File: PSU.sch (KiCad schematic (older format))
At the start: 45 parts, among them J10 1053091202, Q5 BSS84PH6327XTSA2, Q6 IRF7416TRPBF, U13 AP62301WU-7, U14 AP62301WU-7, U15 AP62301WU-7, U16 LMV431IM5, U17 AP62301WU-7

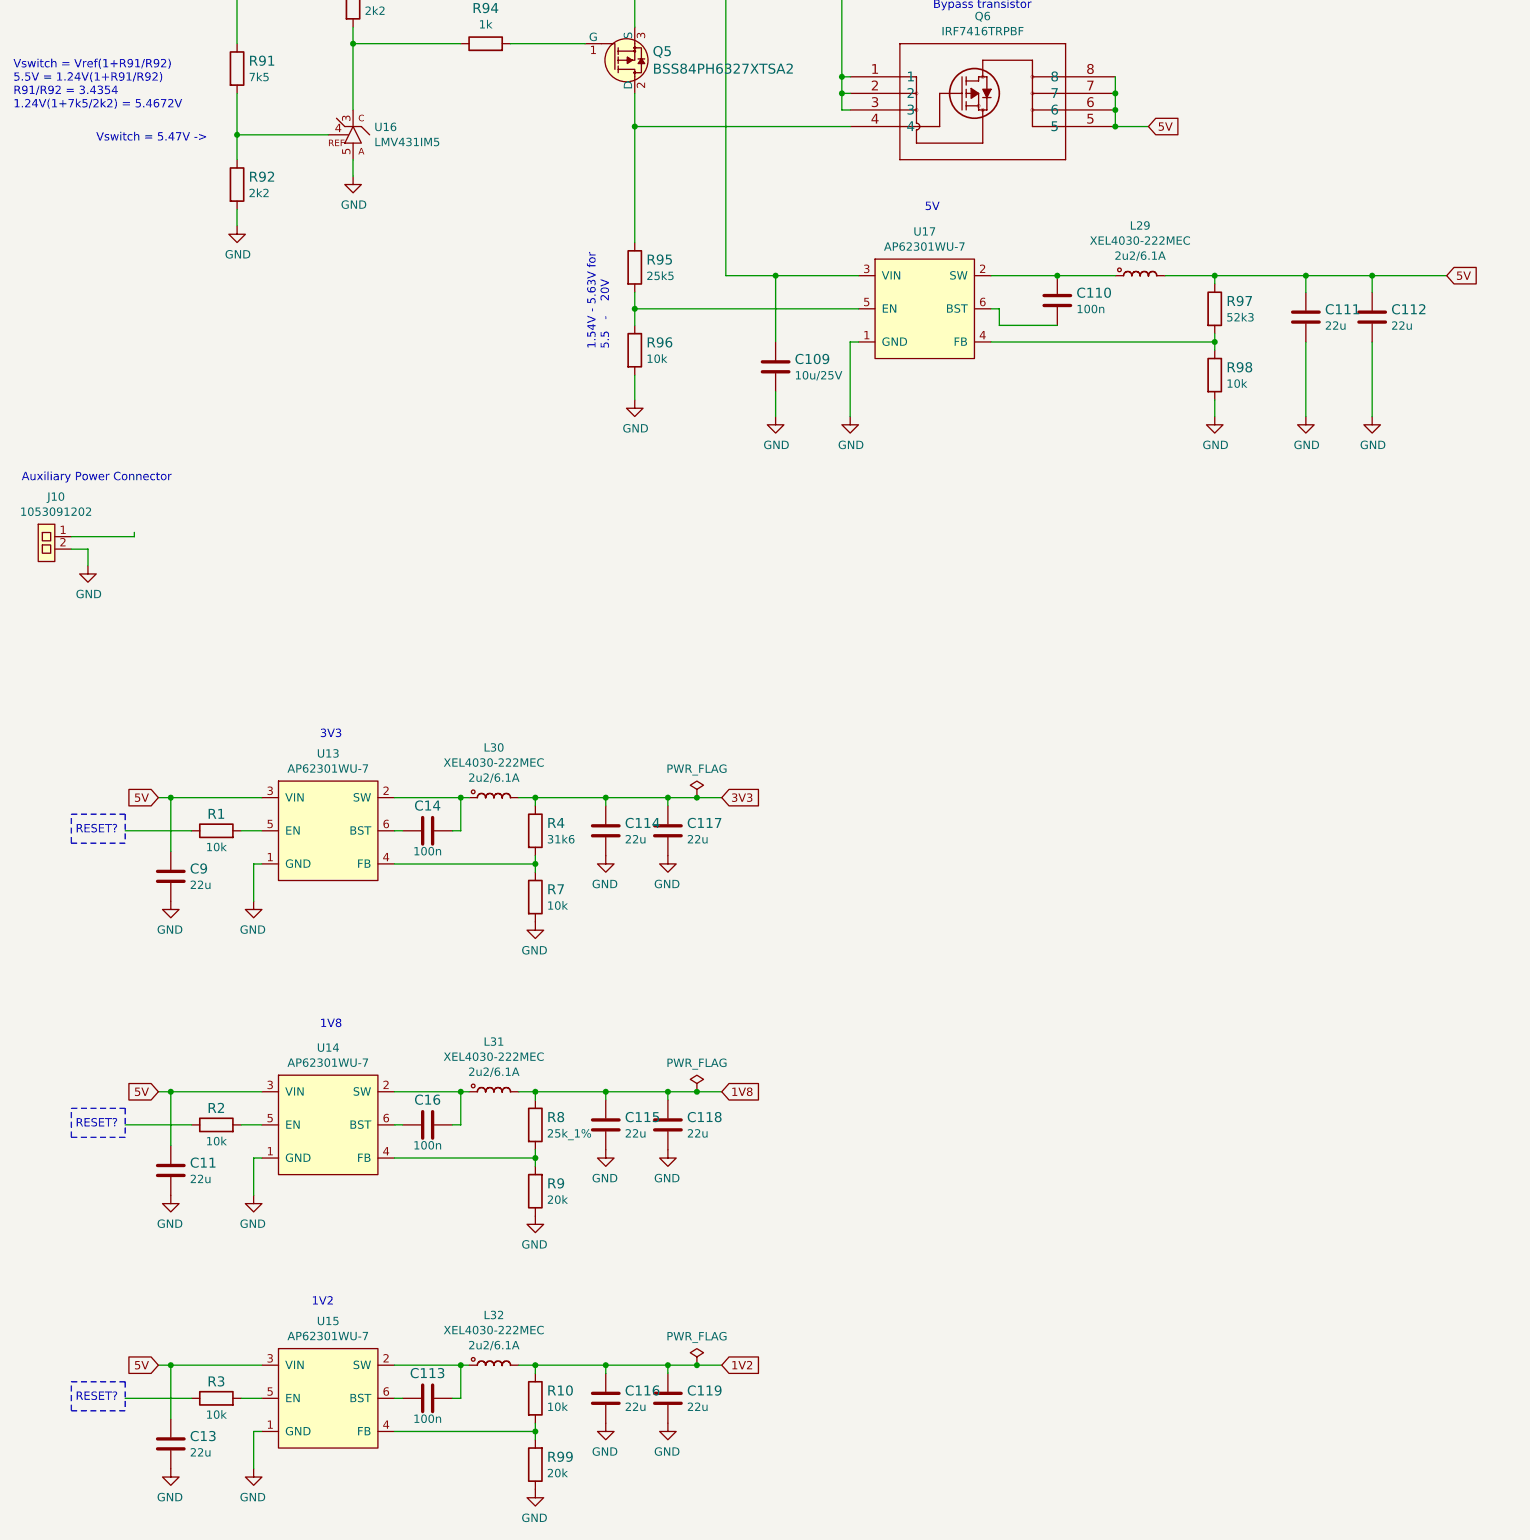
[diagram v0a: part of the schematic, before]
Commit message: Cleanup PoE.sch, change names of power lines
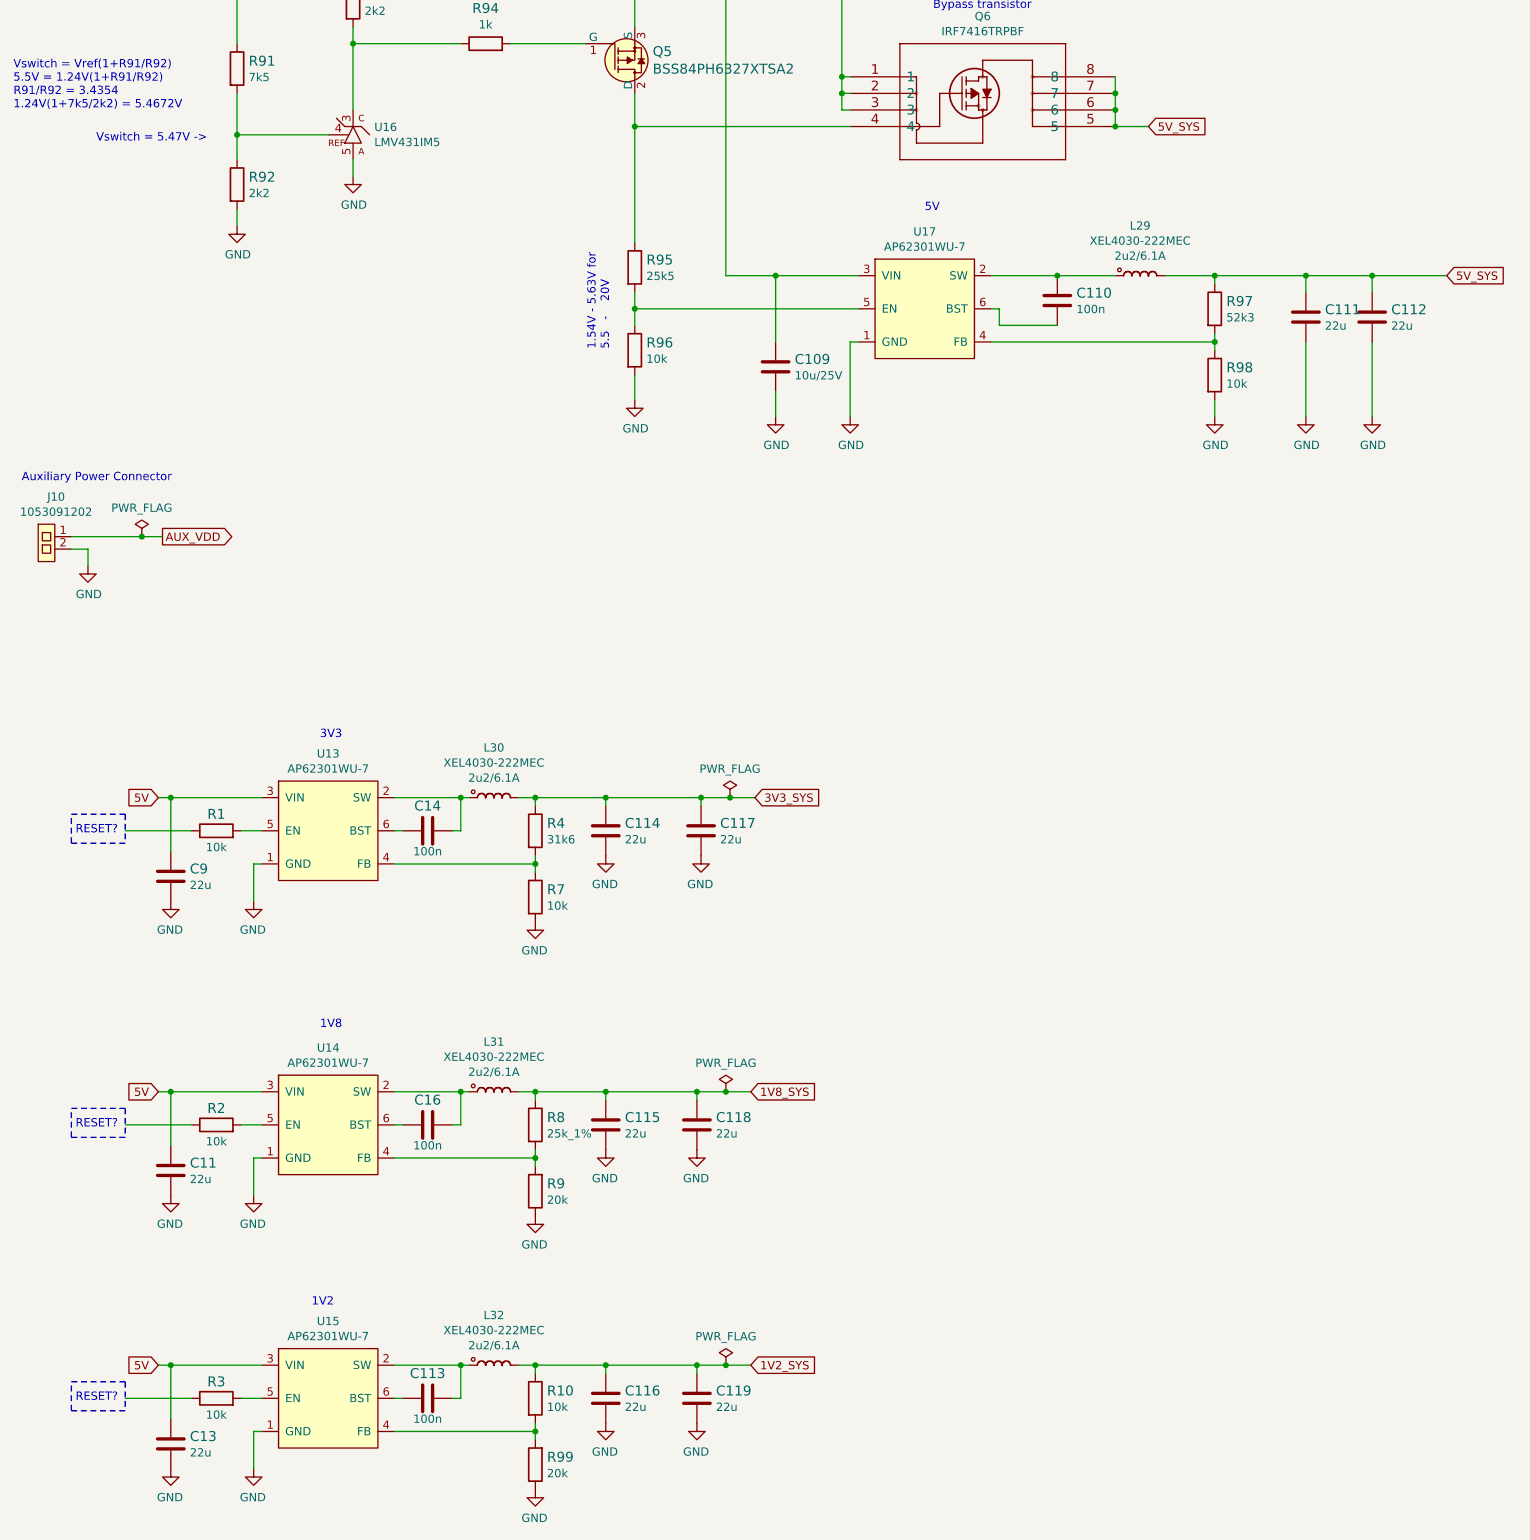
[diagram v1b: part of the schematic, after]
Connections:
- net labels added: 1V2_SYS, 1V8_SYS, 3V3_SYS, 5V_SYS, AUX_VDD
- net labels removed: 1V2, 1V8, 3V3
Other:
- moved on the sheet: C117, C118, C119
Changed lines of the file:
@@
 Auxiliary Power Connector
-Wire Wire Line
-	1580 4575 1580 4549
-Wire Wire Line
-	1200 4575 1580 4575
 Wire Wire Line
 	1300 4650 1200 4650
@@
 $EndComp
 Text GLabel 7700 2100 2    50   Input ~ 0
-5V
+5V_SYS
 $Comp
 L sa800u-baseboard-hw:C_100n_0402 C110
@@
 Connection ~ 9050 3000
 Text GLabel 9500 3000 2    50   Input ~ 0
-5V
+5V_SYS
 Wire Wire Line
 	7800 3000 8100 3000
@@
 	1    0    0    -1
 $EndComp
-Wire Wire Line
-	4425 9575 4800 9575
-Connection ~ 4800 9575
-Wire Wire Line
-	4800 9625 4800 9575
 $Comp
 L sa800u-baseboard-hw:GND #PWR0188
 U 1 1 61E1B2C0
-P 4800 9925
+P 4975 9925
 AR Path="/61B0DC30/61E1B2C0" Ref="#PWR0188"  Part="1"
 AR Path="/61DC2BE0/61E1B2C0" Ref="#PWR0176"  Part="1"
-F 0 "#PWR0188" H 4800 9675 50  0001 C CNN
-F 1 "GND" H 4805 9752 50  0000 C CNN
-F 2 "" H 4800 9925 50  0001 C CNN
-F 3 "" H 4800 9925 50  0001 C CNN
-	1    4800 9925
+F 0 "#PWR0188" H 4975 9675 50  0001 C CNN
+F 1 "GND" H 4980 9752 50  0000 C CNN
+F 2 "" H 4975 9925 50  0001 C CNN
+F 3 "" H 4975 9925 50  0001 C CNN
+	1    4975 9925
 	-1   0    0    -1
 $EndComp
@@
 L sa800u-baseboard-hw:C_22u_0603 C119
 U 1 1 61E1B2BF
-P 4800 9775
+P 4975 9775
 AR Path="/61B0DC30/61E1B2BF" Ref="C119"  Part="1"
 AR Path="/61DC2BE0/61E1B2BF" Ref="C119"  Part="1"
-F 0 "C119" H 4915 9820 60  0000 L CNN
-F 1 "C_22u_0603" H 4800 9625 60  0001 C CNN
-F 2 "sa800u-baseboard-hw-footprints:0603-cap" H 5000 9975 60  0001 L CNN
-F 3 "" H 4800 9775 50  0001 C CNN
-F 4 "MURATA" H 5000 10175 60  0001 L CNN "Manufacturer"
-F 5 "GRM188R60J226MEA0D" H 5000 10075 60  0001 L CNN "MPN"
-F 6 "22u" H 4915 9722 50  0000 L CNN "Val"
-	1    4800 9775
+F 0 "C119" H 5090 9820 60  0000 L CNN
+F 1 "C_22u_0603" H 4975 9625 60  0001 C CNN
+F 2 "sa800u-baseboard-hw-footprints:0603-cap" H 5175 9975 60  0001 L CNN
+F 3 "" H 4975 9775 50  0001 C CNN
+F 4 "MURATA" H 5175 10175 60  0001 L CNN "Manufacturer"
+F 5 "GRM188R60J226MEA0D" H 5175 10075 60  0001 L CNN "MPN"
+F 6 "22u" H 5090 9722 50  0000 L CNN "Val"
+	1    4975 9775
 	1    0    0    -1
 $EndComp
@@
 5V
 Wire Wire Line
-	4975 9575 5125 9575
-Wire Wire Line
-	4800 9575 4975 9575
-Connection ~ 4975 9575
+	5150 9575 5300 9575
+Connection ~ 5150 9575
 $Comp
 L sa800u-baseboard-hw:PWR_FLAG #FLG0107
 U 1 1 61E20376
-P 4975 9575
+P 5150 9575
 AR Path="/61B0DC30/61E20376" Ref="#FLG0107"  Part="1"
 AR Path="/61DC2BE0/61E20376" Ref="#FLG0102"  Part="1"
-F 0 "#FLG0107" H 4975 9650 50  0001 C CNN
-F 1 "PWR_FLAG" H 4975 9748 50  0000 C CNN
-F 2 "" H 4975 9575 50  0001 C CNN
-F 3 "~" H 4975 9575 50  0001 C CNN
-	1    4975 9575
+F 0 "#FLG0107" H 5150 9650 50  0001 C CNN
+F 1 "PWR_FLAG" H 5150 9748 50  0000 C CNN
+F 2 "" H 5150 9575 50  0001 C CNN
+F 3 "~" H 5150 9575 50  0001 C CNN
+	1    5150 9575
 	1    0    0    -1
 $EndComp
@@
 	1    0    0    -1
 $EndComp
-Wire Wire Line
-	4425 7925 4800 7925
-Connection ~ 4800 7925
-Wire Wire Line
-	4800 7975 4800 7925
+Connection ~ 4975 7925
+Wire Wire Line
+	4975 7975 4975 7925
 $Comp
 L sa800u-baseboard-hw:GND #PWR0219
 U 1 1 61E1B2B8
-P 4800 8275
+P 4975 8275
 AR Path="/61B0DC30/61E1B2B8" Ref="#PWR0219"  Part="1"
 AR Path="/61DC2BE0/61E1B2B8" Ref="#PWR0171"  Part="1"
-F 0 "#PWR0219" H 4800 8025 50  0001 C CNN
-F 1 "GND" H 4805 8102 50  0000 C CNN
-F 2 "" H 4800 8275 50  0001 C CNN
-F 3 "" H 4800 8275 50  0001 C CNN
-	1    4800 8275
+F 0 "#PWR0219" H 4975 8025 50  0001 C CNN
+F 1 "GND" H 4980 8102 50  0000 C CNN
+F 2 "" H 4975 8275 50  0001 C CNN
+F 3 "" H 4975 8275 50  0001 C CNN
+	1    4975 8275
 	-1   0    0    -1
 $EndComp
@@
 L sa800u-baseboard-hw:C_22u_0603 C118
 U 1 1 61E6AE12
-P 4800 8125
+P 4975 8125
 AR Path="/61B0DC30/61E6AE12" Ref="C118"  Part="1"
 AR Path="/61DC2BE0/61E6AE12" Ref="C118"  Part="1"
-F 0 "C118" H 4915 8170 60  0000 L CNN
-F 1 "C_22u_0603" H 4800 7975 60  0001 C CNN
-F 2 "sa800u-baseboard-hw-footprints:0603-cap" H 5000 8325 60  0001 L CNN
-F 3 "" H 4800 8125 50  0001 C CNN
-F 4 "MURATA" H 5000 8525 60  0001 L CNN "Manufacturer"
-F 5 "GRM188R60J226MEA0D" H 5000 8425 60  0001 L CNN "MPN"
-F 6 "22u" H 4915 8072 50  0000 L CNN "Val"
-	1    4800 8125
+F 0 "C118" H 5090 8170 60  0000 L CNN
+F 1 "C_22u_0603" H 4975 7975 60  0001 C CNN
+F 2 "sa800u-baseboard-hw-footprints:0603-cap" H 5175 8325 60  0001 L CNN
+F 3 "" H 4975 8125 50  0001 C CNN
+F 4 "MURATA" H 5175 8525 60  0001 L CNN "Manufacturer"
+F 5 "GRM188R60J226MEA0D" H 5175 8425 60  0001 L CNN "MPN"
+F 6 "22u" H 5090 8072 50  0000 L CNN "Val"
+	1    4975 8125
 	1    0    0    -1
 $EndComp
@@
 Wire Wire Line
 	4000 8325 4000 8275
-Connection ~ 4425 7925
 Wire Wire Line
 	4000 7925 4425 7925
@@
 5V
 Wire Wire Line
-	4975 7925 5125 7925
-Wire Wire Line
-	4800 7925 4975 7925
-Connection ~ 4975 7925
+	5150 7925 5300 7925
+Wire Wire Line
+	4975 7925 5150 7925
+Connection ~ 5150 7925
 $Comp
 L sa800u-baseboard-hw:PWR_FLAG #FLG0122
 U 1 1 61E6AE0F
-P 4975 7925
+P 5150 7925
 AR Path="/61B0DC30/61E6AE0F" Ref="#FLG0122"  Part="1"
 AR Path="/61DC2BE0/61E6AE0F" Ref="#FLG0101"  Part="1"
-F 0 "#FLG0122" H 4975 8000 50  0001 C CNN
-F 1 "PWR_FLAG" H 4975 8098 50  0000 C CNN
-F 2 "" H 4975 7925 50  0001 C CNN
-F 3 "~" H 4975 7925 50  0001 C CNN
-	1    4975 7925
+F 0 "#FLG0122" H 5150 8000 50  0001 C CNN
+F 1 "PWR_FLAG" H 5150 8098 50  0000 C CNN
+F 2 "" H 5150 7925 50  0001 C CNN
+F 3 "~" H 5150 7925 50  0001 C CNN
+	1    5150 7925
 	1    0    0    -1
 $EndComp
@@
 	1    0    0    -1
 $EndComp
-Wire Wire Line
-	4425 6150 4800 6150
-Connection ~ 4800 6150
-Wire Wire Line
-	4800 6200 4800 6150
+Connection ~ 5000 6150
+Wire Wire Line
+	5000 6200 5000 6150
 $Comp
 L sa800u-baseboard-hw:GND #PWR0224
 U 1 1 61E6AE0D
-P 4800 6500
+P 5000 6500
 AR Path="/61B0DC30/61E6AE0D" Ref="#PWR0224"  Part="1"
 AR Path="/61DC2BE0/61E6AE0D" Ref="#PWR0166"  Part="1"
-F 0 "#PWR0224" H 4800 6250 50  0001 C CNN
-F 1 "GND" H 4805 6327 50  0000 C CNN
-F 2 "" H 4800 6500 50  0001 C CNN
-F 3 "" H 4800 6500 50  0001 C CNN
-	1    4800 6500
+F 0 "#PWR0224" H 5000 6250 50  0001 C CNN
+F 1 "GND" H 5005 6327 50  0000 C CNN
+F 2 "" H 5000 6500 50  0001 C CNN
+F 3 "" H 5000 6500 50  0001 C CNN
+	1    5000 6500
 	-1   0    0    -1
 $EndComp
@@
 L sa800u-baseboard-hw:C_22u_0603 C117
 U 1 1 61E1B2CA
-P 4800 6350
+P 5000 6350
 AR Path="/61B0DC30/61E1B2CA" Ref="C117"  Part="1"
 AR Path="/61DC2BE0/61E1B2CA" Ref="C117"  Part="1"
-F 0 "C117" H 4915 6395 60  0000 L CNN
-F 1 "C_22u_0603" H 4800 6200 60  0001 C CNN
-F 2 "sa800u-baseboard-hw-footprints:0603-cap" H 5000 6550 60  0001 L CNN
-F 3 "" H 4800 6350 50  0001 C CNN
-F 4 "MURATA" H 5000 6750 60  0001 L CNN "Manufacturer"
-F 5 "GRM188R60J226MEA0D" H 5000 6650 60  0001 L CNN "MPN"
-F 6 "22u" H 4915 6297 50  0000 L CNN "Val"
-	1    4800 6350
+F 0 "C117" H 5115 6395 60  0000 L CNN
+F 1 "C_22u_0603" H 5000 6200 60  0001 C CNN
+F 2 "sa800u-baseboard-hw-footprints:0603-cap" H 5200 6550 60  0001 L CNN
+F 3 "" H 5000 6350 50  0001 C CNN
+F 4 "MURATA" H 5200 6750 60  0001 L CNN "Manufacturer"
+F 5 "GRM188R60J226MEA0D" H 5200 6650 60  0001 L CNN "MPN"
+F 6 "22u" H 5115 6297 50  0000 L CNN "Val"
+	1    5000 6350
 	1    0    0    -1
 $EndComp
@@
 Wire Wire Line
 	4000 6550 4000 6500
-Connection ~ 4425 6150
 Wire Wire Line
 	4000 6150 4425 6150
@@
 Text GLabel 1725 6150 0    50   Input ~ 0
 5V
-Text GLabel 5125 7925 2    50   Input ~ 0
-1V8
-Wire Wire Line
-	4975 6150 5125 6150
-Wire Wire Line
-	4800 6150 4975 6150
-Connection ~ 4975 6150
+Text GLabel 5300 7925 2    50   Input ~ 0
+1V8_SYS
+Wire Wire Line
+	5175 6150 5325 6150
+Wire Wire Line
+	5000 6150 5175 6150
+Connection ~ 5175 6150
 $Comp
 L sa800u-baseboard-hw:PWR_FLAG #FLG0123
 U 1 1 61E1B2AE
-P 4975 6150
+P 5175 6150
 AR Path="/61B0DC30/61E1B2AE" Ref="#FLG0123"  Part="1"
 AR Path="/61DC2BE0/61E1B2AE" Ref="#FLG0103"  Part="1"
-F 0 "#FLG0123" H 4975 6225 50  0001 C CNN
-F 1 "PWR_FLAG" H 4975 6323 50  0000 C CNN
-F 2 "" H 4975 6150 50  0001 C CNN
-F 3 "~" H 4975 6150 50  0001 C CNN
-	1    4975 6150
-	1    0    0    -1
-$EndComp
-Text GLabel 5125 9575 2    50   Input ~ 0
-1V2
-Text GLabel 5125 6150 2    50   Input ~ 0
-3V3
+F 0 "#FLG0123" H 5175 6225 50  0001 C CNN
+F 1 "PWR_FLAG" H 5175 6323 50  0000 C CNN
+F 2 "" H 5175 6150 50  0001 C CNN
+F 3 "~" H 5175 6150 50  0001 C CNN
+	1    5175 6150
+	1    0    0    -1
+$EndComp
+Text GLabel 5300 9575 2    50   Input ~ 0
+1V2_SYS
+Text GLabel 5325 6150 2    50   Input ~ 0
+3V3_SYS
 $Comp
 L sa800u-baseboard-hw:AP62301WU-7 U13
@@
 Text Notes 2700 5800 0    50   ~ 0
 3V3
+Connection ~ 4975 9575
+Wire Wire Line
+	4975 9575 5150 9575
+Wire Wire Line
+	4975 9575 4975 9625
+Wire Wire Line
+	4425 9575 4975 9575
+Wire Wire Line
+	4425 7925 4975 7925
+Connection ~ 4425 7925
+Wire Wire Line
+	4425 6150 5000 6150
+Connection ~ 4425 6150
+Text GLabel 1750 4575 2    50   Output ~ 0
+AUX_VDD
+$Comp
+L sa800u-baseboard-hw:PWR_FLAG #FLG?
+U 1 1 663ECDD9
+P 1625 4575
+AR Path="/61B0DC30/663ECDD9" Ref="#FLG?"  Part="1"
+AR Path="/61DC2BE0/663ECDD9" Ref="#FLG?"  Part="1"
+F 0 "#FLG?" H 1625 4650 50  0001 C CNN
+F 1 "PWR_FLAG" H 1625 4748 50  0000 C CNN
+F 2 "" H 1625 4575 50  0001 C CNN
+F 3 "~" H 1625 4575 50  0001 C CNN
+	1    1625 4575
+	1    0    0    -1
+$EndComp
+Wire Wire Line
+	1200 4575 1625 4575
+Connection ~ 1625 4575
+Wire Wire Line
+	1625 4575 1750 4575
 $EndSCHEMATC

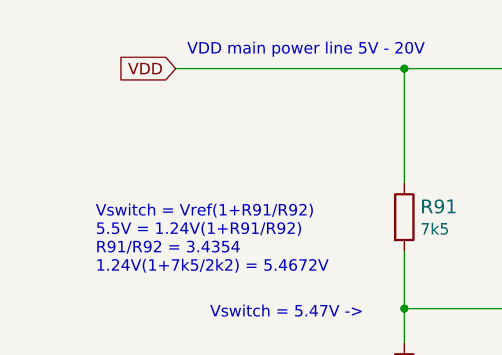
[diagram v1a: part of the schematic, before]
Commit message: Update power labels
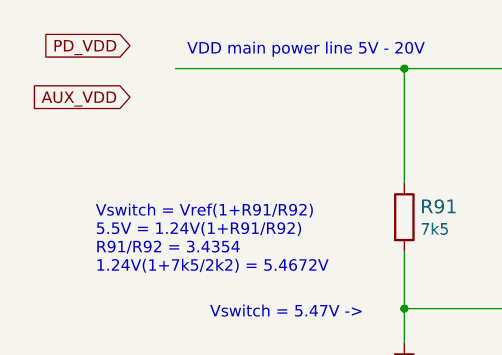
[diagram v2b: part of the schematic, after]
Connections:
- net labels added: PD_VDD
- net labels removed: VDD
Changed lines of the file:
@@
 Text Notes 6350 2700 0    50   ~ 0
 5V\n\n
-Text GLabel 1200 1100 0    50   Input ~ 0
-VDD
 Wire Wire Line
 	2200 2600 2200 2700
@@
 Wire Wire Line
 	1625 4575 1750 4575
+Text GLabel 1000 1225 0    50   Input ~ 0
+AUX_VDD
+Text GLabel 1000 1000 0    50   Input ~ 0
+PD_VDD
 $EndSCHEMATC
